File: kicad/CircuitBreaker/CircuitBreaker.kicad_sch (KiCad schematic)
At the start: 33 parts

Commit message: pwr and up/down link
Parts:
- added C?: 100uF, symbol Device:C_Polarized_US
- added J?: 5V, symbol Connector:Screw_Terminal_01x02
- added J?: Conn_01x04_downlink, symbol Connector:Conn_01x04_Female
- added J?: JUMP, symbol Connector:Screw_Terminal_01x02
- added J?: Conn_01x04_uplink, symbol Connector:Conn_01x04_Female
- added JP? (x2): I2C, symbol Jumper:SolderJumper_2_Open
- added JP? (x2): dbg-sel, symbol Jumper:SolderJumper_2_Open
- added JP? (x2): bus-type, symbol Jumper:SolderJumper_3_Open
- added R? (x4): 10K, symbol Device:R
- added R? (x2): 22, symbol Device:R
- added U?: AP1117-33, Package_TO_SOT_SMD:SOT-223-3_TabPin2, symbol Regulator_Linear:AP1117-33
- added U?: LM324, symbol Amplifier_Operational:LM324
- added U?: ESP-12E, RF_Module:ESP-12E, symbol RF_Module:ESP-12E
- J?: value Conn_01x04_Female -> Conn_01x04_uplink
- J?: value Conn_01x04_Female -> Conn_01x04_downlink
- R? (x4): value 250 -> 240_0805
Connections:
- net +5V: now also J?.1 (Pin_1), J?.2 (Pin_2), J?.2 (Pin_2), U?.3 (VI), U?.4 (V+); no longer J?.1 (Pin_1)
- net GND: now also C?.2, J?.1 (Pin_1), J?.4 (Pin_4), J?.4 (Pin_4), U?.1 (GND), U?.11 (V-), U?.15 (GND)
- net RXD_DWN: now also J?.3 (Pin_3), JP?.2 (C), R?.2
- net RXD_UP: now also J?.2 (Pin_2), JP?.1 (A), JP?.2 (B), R?.2, R?.2
- net TXD_DWN: now also J?.2 (Pin_2), JP?.2 (C), R?.2
- net TXD_UP: now also J?.3 (Pin_3), JP?.1 (A), JP?.2 (B), R?.2, R?.2
- new net: JP?.2 (B), U?.21 (GPIO3/RXD)
- new net: JP?.2 (B), U?.22 (GPIO1/TXD)
- new net +3V3: C?.1, J?.1 (Pin_1), J?.1 (Pin_1), J?.1 (Pin_1), R?.1, R?.1, R?.1, R?.1, U?.2 (VO), U?.8 (VCC)
- new net DRXD: JP?.1 (A)
- new net DTXD: JP?.1 (A)
- new net P3.0: R?.1
- new net P3.1: R?.1
- new net SDA: JP?.1 (A), JP?.3 (B)
- new net SDL: JP?.1 (A), JP?.3 (B)
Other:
- moved on the sheet: C?, J?, R?, T?, U?, U?A, U?B, U?C, U?D

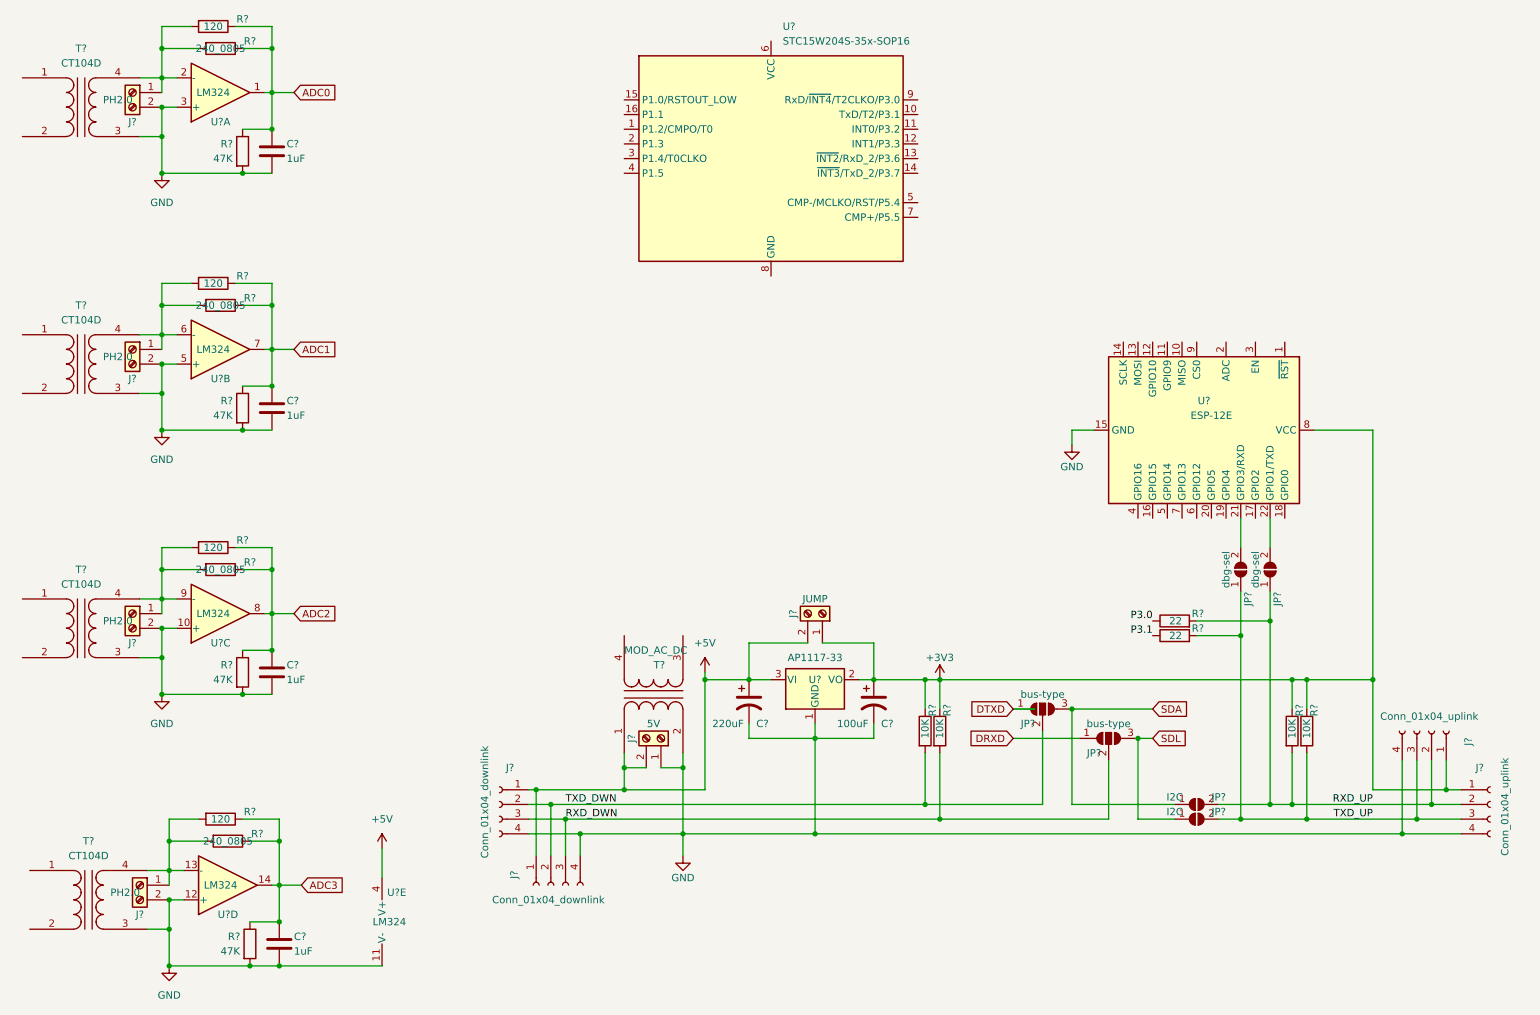
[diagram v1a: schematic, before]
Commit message: sch-erc checked
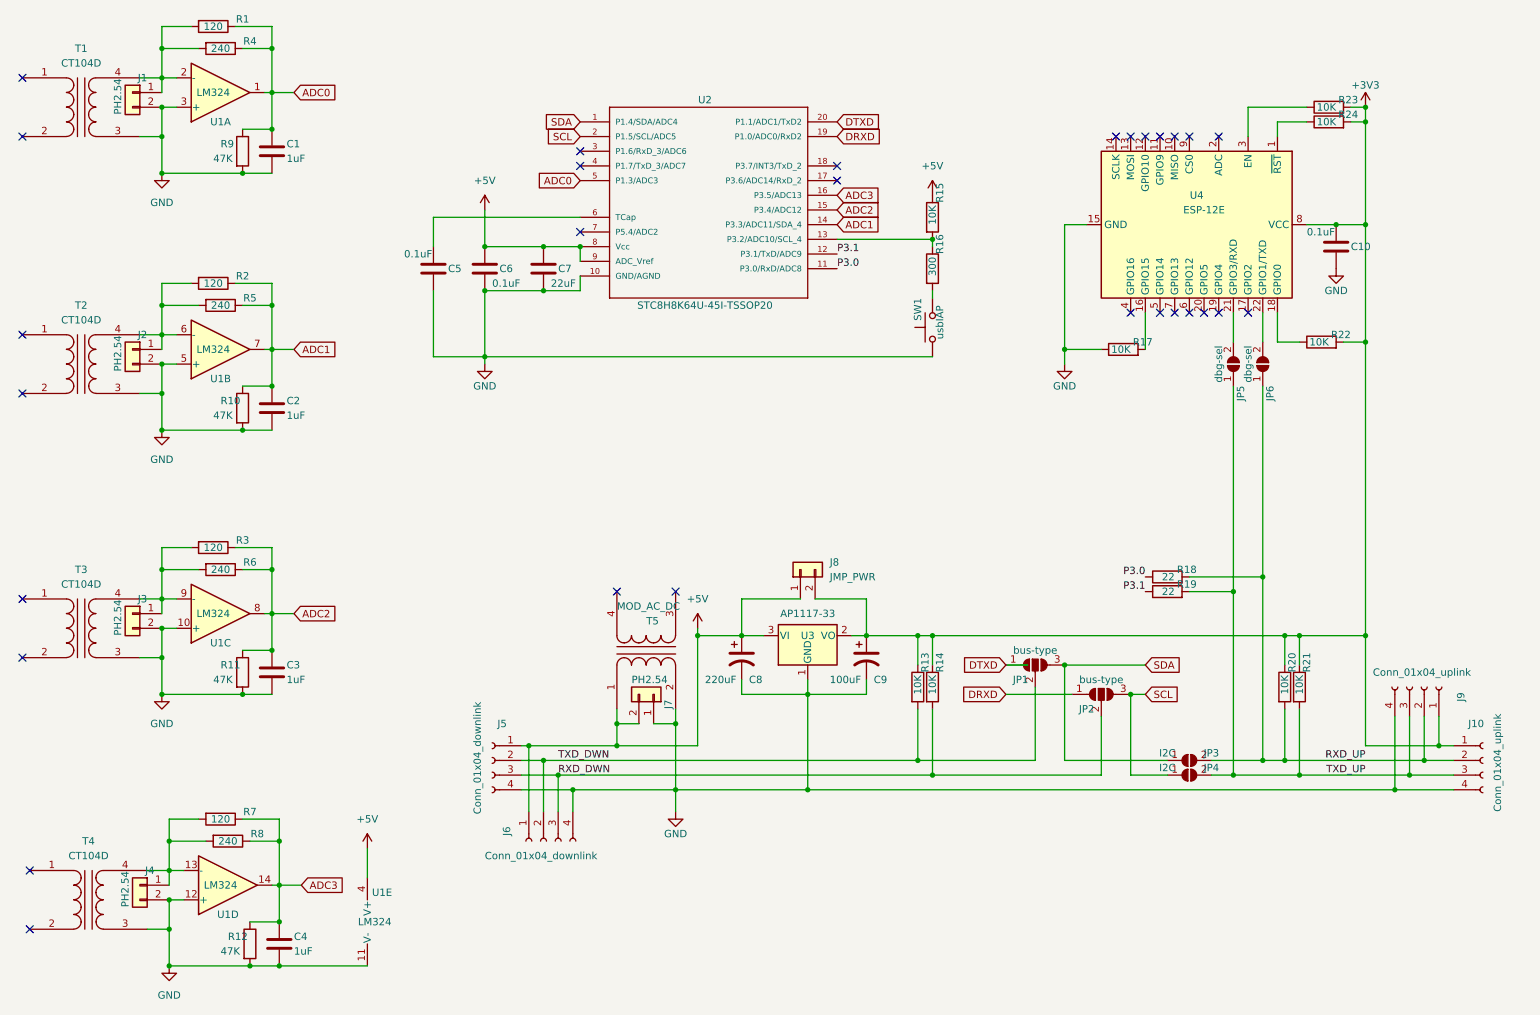
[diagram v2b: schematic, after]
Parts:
- removed J? (x4): PH2.0, symbol Connector:Screw_Terminal_01x02
- removed J?: 5V, symbol Connector:Screw_Terminal_01x02
- removed J?: JUMP, symbol Connector:Screw_Terminal_01x02
- removed R? (x3): 240_0805, symbol Device:R
- removed U?: STC15W204S-35x-SOP16, Package_SO:STC_SOP-16_3.9x9.9mm_P1.27mm, symbol MCU_STC:STC15W204S-35x-SOP16
- added C10, C5, C6: 0.1uF, symbol Device:C
- added C7: 22uF, symbol Device:C
- added J1, J2, J3, J4, J7: PH2.54, symbol Connector_Generic:Conn_01x02
- added J8: JMP_PWR, symbol Connector_Generic:Conn_01x02
- added R15, R17, R22, R23, R24: 10K, symbol Device:R
- added R16: 300, symbol Device:R
- added R4, R6, R8: 240, Resistor_SMD:R_0805_2012Metric, symbol Device:R
- added SW1: usbIAP, symbol Switch:SW_Push
- added U2: STC8H8K64U-45I-TSSOP20, symbol MCU-HT:STC8Hnnn20P
- R5: renamed from R?; value 240_0805 -> 240; footprint (none) -> Resistor_SMD:R_0805_2012Metric
- gave numbers to parts that had none: 38
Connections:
- net +3V3: now also C10.1, J8.2 (Pin_2), R22.2, R23.2, R24.2
- net +5V: now also C6.1, C7.1, J7.2 (Pin_2), J8.1 (Pin_1), R15.1, U2.8 (Vcc), U2.9 (ADC_Vref)
- net ADC0: now also R4.1, U2.5 (P1.3/ADC3)
- net ADC1: now also U2.14 (P3.3/ADC11/SDA_4)
- net ADC2: now also R6.1, U2.15 (P3.4/ADC12)
- net ADC3: now also R8.1, U2.16 (P3.5/ADC13)
- net DRXD: now also U2.19 (P1.0/ADC0/RxD2)
- net DTXD: now also U2.20 (P1.1/ADC1/TxD2)
- net GND: now also C10.2, C5.2, C6.2, C7.2, J1.2 (Pin_2), J2.2 (Pin_2), J3.2 (Pin_2), J4.2 (Pin_2), J7.1 (Pin_1), R17.1, SW1.1, U2.10 (GND/AGND)
- net P3.0: now also U2.11 (P3.0/RxD/ADC8)
- net P3.1: now also U2.12 (P3.1/TxD/ADC9)
- net SDA: now also U2.1 (P1.4/SDA/ADC4)
- net at R7.2, T4.4 (SB), U1.13 (-): now also J4.1 (Pin_1), R8.2
- net at R1.2, T1.4 (SB), U1.2 (-): now also J1.1 (Pin_1), R4.2
- net at R3.2, T3.4 (SB), U1.9 (-): now also J3.1 (Pin_1), R6.2
- net at R2.2, R5.2, T2.4 (SB)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: now also J2.1 (Pin_1)
- net at U4.1 (~{RST}): now also R24.1
- net at U4.16 (GPIO15): now also R17.2
- net at U4.18 (GPIO0): now also R22.1
- net at U4.3 (EN): now also R23.1
- net SDL renamed SCL
- net SCL: now also U2.2 (P1.5/SCL/ADC5)
- new net: C5.1, U2.6 (TCap)
- new net: R15.2, R16.1, U2.13 (P3.2/ADC10/SCL_4)
- new net: R16.2, SW1.2
- no-connect marks 0 -> 29
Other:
- moved on the sheet: C8, C9, J10, J5, J6, J9, JP1, JP2, JP3, JP4, JP5, JP6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

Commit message: ccb pcb rev
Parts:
- removed J2, J3: PH2.54, symbol Connector_Generic:Conn_01x02
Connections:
- net +5V: now also J7.1 (Pin_1); no longer J7.2 (Pin_2)
- net GND: now also J7.2 (Pin_2); no longer J7.1 (Pin_1)
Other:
- moved on the sheet: J7
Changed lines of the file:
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@@
   (junction (at 262.89 152.4) (diameter 0) (color 0 0 0 0)
   )
-  (junction (at 49.53 124.46) (diameter 0) (color 0 0 0 0)
-  )
   (junction (at 69.85 182.88) (diameter 0) (color 0 0 0 0)
   )
@@
   )
   (junction (at 105.41 77.47) (diameter 0) (color 0 0 0 0)
-  )
-  (junction (at 49.53 78.74) (diameter 0) (color 0 0 0 0)
   )
   (junction (at 234.95 149.86) (diameter 0) (color 0 0 0 0)
@@
     (stroke (width 0) (type default) (color 0 0 0 0))
   )
-  (wire (pts (xy 49.53 73.66) (xy 49.53 76.2))
-    (stroke (width 0) (type default) (color 0 0 0 0))
-  )
   (wire (pts (xy 96.52 77.47) (xy 105.41 77.47))
     (stroke (width 0) (type default) (color 0 0 0 0))
@@
   )
   (wire (pts (xy 54.61 110.49) (xy 49.53 110.49))
-    (stroke (width 0) (type default) (color 0 0 0 0))
-  )
-  (wire (pts (xy 49.53 119.38) (xy 49.53 121.92))
     (stroke (width 0) (type default) (color 0 0 0 0))
   )
@@
     (pin "4")
   )
-  (symbol (lib_id "Connector_Generic:Conn_01x02") (at 44.45 121.92 0) (mirror y) (unit 1)
-    (in_bom yes) (on_board yes)
-    (property "Reference" "J3" (id 0) (at 46.99 119.38 0)
-      (effects (font (size 1.27 1.27)) (justify left))
-    )
-    (property "Value" "PH2.54" (id 1) (at 41.91 125.73 90)
-      (effects (font (size 1.27 1.27)) (justify left))
-    )
-    (property "Footprint" "" (id 2) (at 44.45 121.92 0)
-      (effects (font (size 1.27 1.27)) hide)
-    )
-    (property "Datasheet" "~" (id 3) (at 44.45 121.92 0)
-      (effects (font (size 1.27 1.27)) hide)
-    )
-    (pin "1")
-    (pin "2")
-  )
-  (symbol (lib_id "Connector_Generic:Conn_01x02") (at 134.62 135.89 270) (mirror x) (unit 1)
-    (in_bom yes) (on_board yes)
-    (property "Reference" "J7" (id 0) (at 137.16 138.43 0)
-      (effects (font (size 1.27 1.27)) (justify left))
-    )
-    (property "Value" "PH2.54" (id 1) (at 130.81 133.35 90)
-      (effects (font (size 1.27 1.27)) (justify left))
-    )
-    (property "Footprint" "" (id 2) (at 134.62 135.89 0)
-      (effects (font (size 1.27 1.27)) hide)
-    )
-    (property "Datasheet" "~" (id 3) (at 134.62 135.89 0)
+  (symbol (lib_id "Connector_Generic:Conn_01x02") (at 132.08 135.89 90) (unit 1)
+    (in_bom yes) (on_board yes)
+    (property "Reference" "J7" (id 0) (at 129.54 138.43 0)
+      (effects (font (size 1.27 1.27)) (justify left))
+    )
+    (property "Value" "PH2.54" (id 1) (at 135.89 133.35 90)
+      (effects (font (size 1.27 1.27)) (justify left))
+    )
+    (property "Footprint" "" (id 2) (at 132.08 135.89 0)
+      (effects (font (size 1.27 1.27)) hide)
+    )
+    (property "Datasheet" "~" (id 3) (at 132.08 135.89 0)
       (effects (font (size 1.27 1.27)) hide)
     )
@@
     (pin "2")
   )
-  (symbol (lib_id "Connector_Generic:Conn_01x02") (at 44.45 76.2 0) (mirror y) (unit 1)
-    (in_bom yes) (on_board yes)
-    (property "Reference" "J2" (id 0) (at 46.99 73.66 0)
-      (effects (font (size 1.27 1.27)) (justify left))
-    )
-    (property "Value" "PH2.54" (id 1) (at 41.91 80.01 90)
-      (effects (font (size 1.27 1.27)) (justify left))
-    )
-    (property "Footprint" "" (id 2) (at 44.45 76.2 0)
-      (effects (font (size 1.27 1.27)) hide)
-    )
-    (property "Datasheet" "~" (id 3) (at 44.45 76.2 0)
-      (effects (font (size 1.27 1.27)) hide)
-    )
-    (pin "1")
-    (pin "2")
-  )
   (symbol (lib_id "Device:R") (at 63.5 132.08 0) (unit 1)
     (in_bom yes) (on_board yes)
@@
       (reference "J1") (unit 1) (value "PH2.54") (footprint "")
     )
-    (path "/7a16ba04-4b94-478f-bb0b-f6f31c2d17c5"
-      (reference "J2") (unit 1) (value "PH2.54") (footprint "")
-    )
-    (path "/3bb8f5a2-1f55-4319-932d-893110ee8e4c"
-      (reference "J3") (unit 1) (value "PH2.54") (footprint "")
-    )
     (path "/193502b3-a5e3-46c9-a7b1-77019833c298"

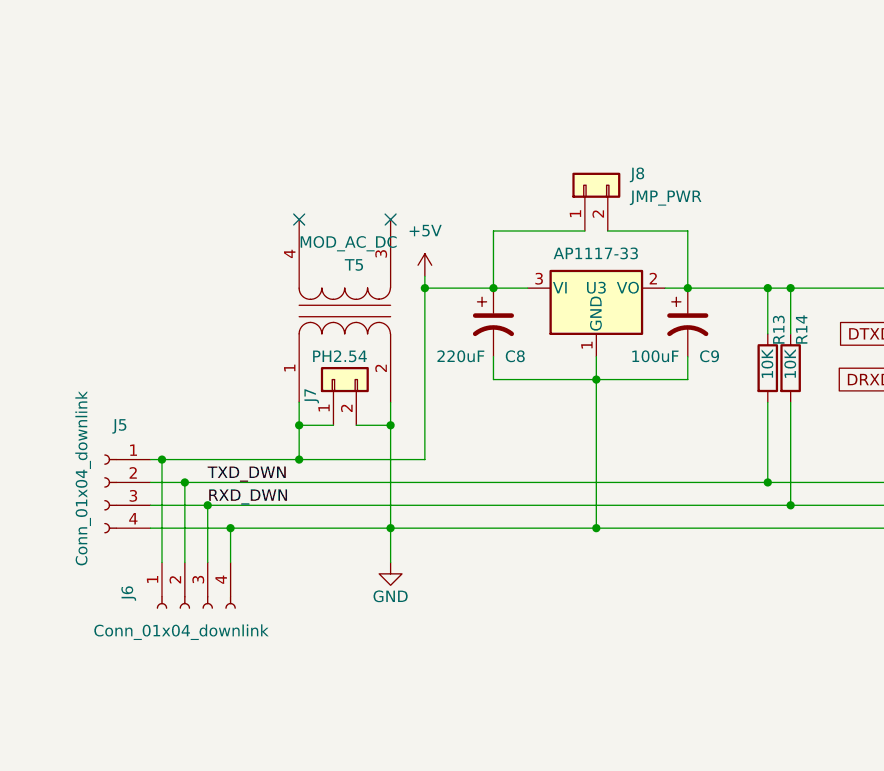
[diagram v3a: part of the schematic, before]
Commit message: footprints applied
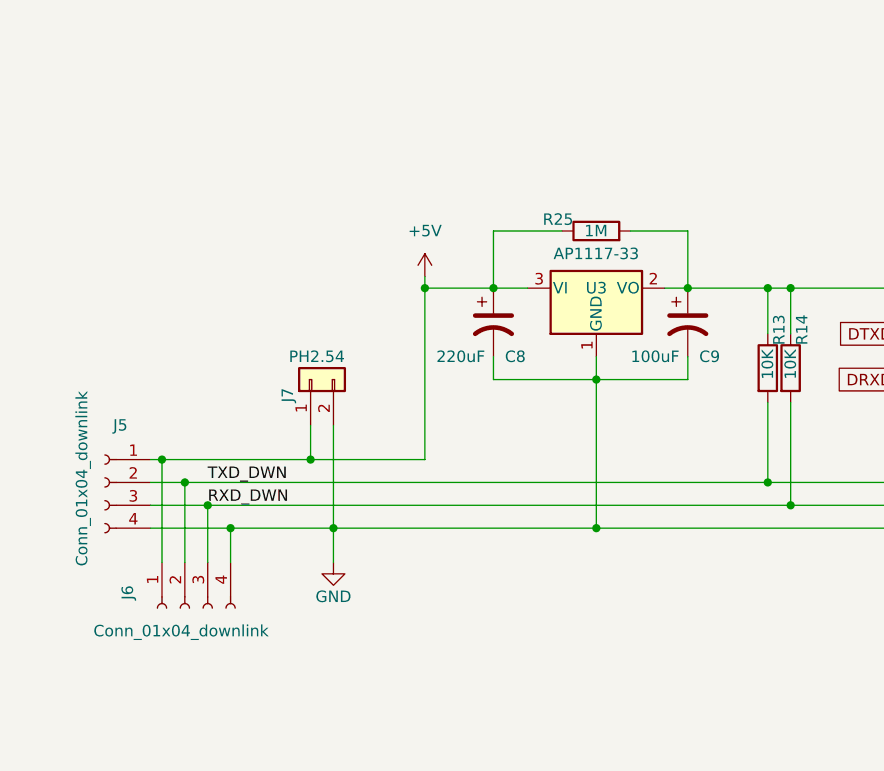
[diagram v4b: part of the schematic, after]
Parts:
- removed J8: JMP_PWR, symbol Connector_Generic:Conn_01x02
- removed T5: MOD_AC_DC, symbol Device:Transformer_1P_1S
- added R25: 1M, Resistor_SMD:R_0805_2012Metric, symbol Device:R
- C1, C10, C2, C3, C4, C5, C6: footprint (none) -> Capacitor_SMD:C_0201_0603Metric
- C7: footprint (none) -> Capacitor_SMD:C_0805_2012Metric
- C8, C9: footprint (none) -> Capacitor_SMD:CP_Elec_6.3x5.2
- J1, J4: footprint (none) -> Connector_PinHeader_2.54mm:PinHeader_1x02_P2.54mm_Vertical
- J10, J9: footprint (none) -> Connector_PinSocket_2.00mm:PinSocket_1x04_P2.00mm_Vertical
- J5, J6: footprint (none) -> Connector_PinHeader_2.00mm:PinHeader_1x04_P2.00mm_Vertical
- J7: footprint (none) -> Connector_PinSocket_2.54mm:PinSocket_1x02_P2.54mm_Vertical_SMD_Pin1Left
- JP1, JP2: footprint (none) -> Jumper:SolderJumper-3_P1.3mm_Bridged2Bar12_RoundedPad1.0x1.5mm_NumberLabels
- JP3, JP4, JP5, JP6: footprint (none) -> Jumper:SolderJumper-2_P1.3mm_Open_RoundedPad1.0x1.5mm
- R1, R2, R3, R7: footprint (none) -> Resistor_THT:R_Axial_DIN0204_L3.6mm_D1.6mm_P1.90mm_Vertical
- R10, R11, R12, R13, R14, R15, R16, R17, R18, R19, R20, R21, R22, R23, R24, R9: footprint (none) -> Resistor_SMD:R_0201_0603Metric
- SW1: footprint (none) -> Button_Switch_SMD:SW_DIP_SPSTx01_Slide_6.7x4.1mm_W6.73mm_P2.54mm_LowProfile_JPin
- T1, T2, T3, T4: footprint (none) -> lib:Transformer_CT204D
- U1: footprint (none) -> lib:SOP-14_3.9x9.9mm_P1.27mm
- U2: footprint (none) -> Package_SO:TSSOP-20_4.4x5mm_P0.4mm
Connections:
- net +3V3: now also R25.2
- net +5V: now also R25.1
- no-connect marks 29 -> 27
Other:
- moved on the sheet: J7
